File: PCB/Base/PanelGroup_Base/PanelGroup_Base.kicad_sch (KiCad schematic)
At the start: 62 parts, among them J1 J_DIAG, J11 J_BREAKOUT, J2 J_BL1, J3 J_I2C2, J4 J_I2C1, J5 J_CAN_TERM, J6 J_BL2, J7 J_SWD, J8 J_BUS_IN, J9 J_BUS_OUT, Q2 IRLML2502, Q3 IRLML2502, SW1 RESET, U1 STM32F103C8Tx, U2 SN65HVD230, U3 AMS1117-3.3, Y1 8MHz

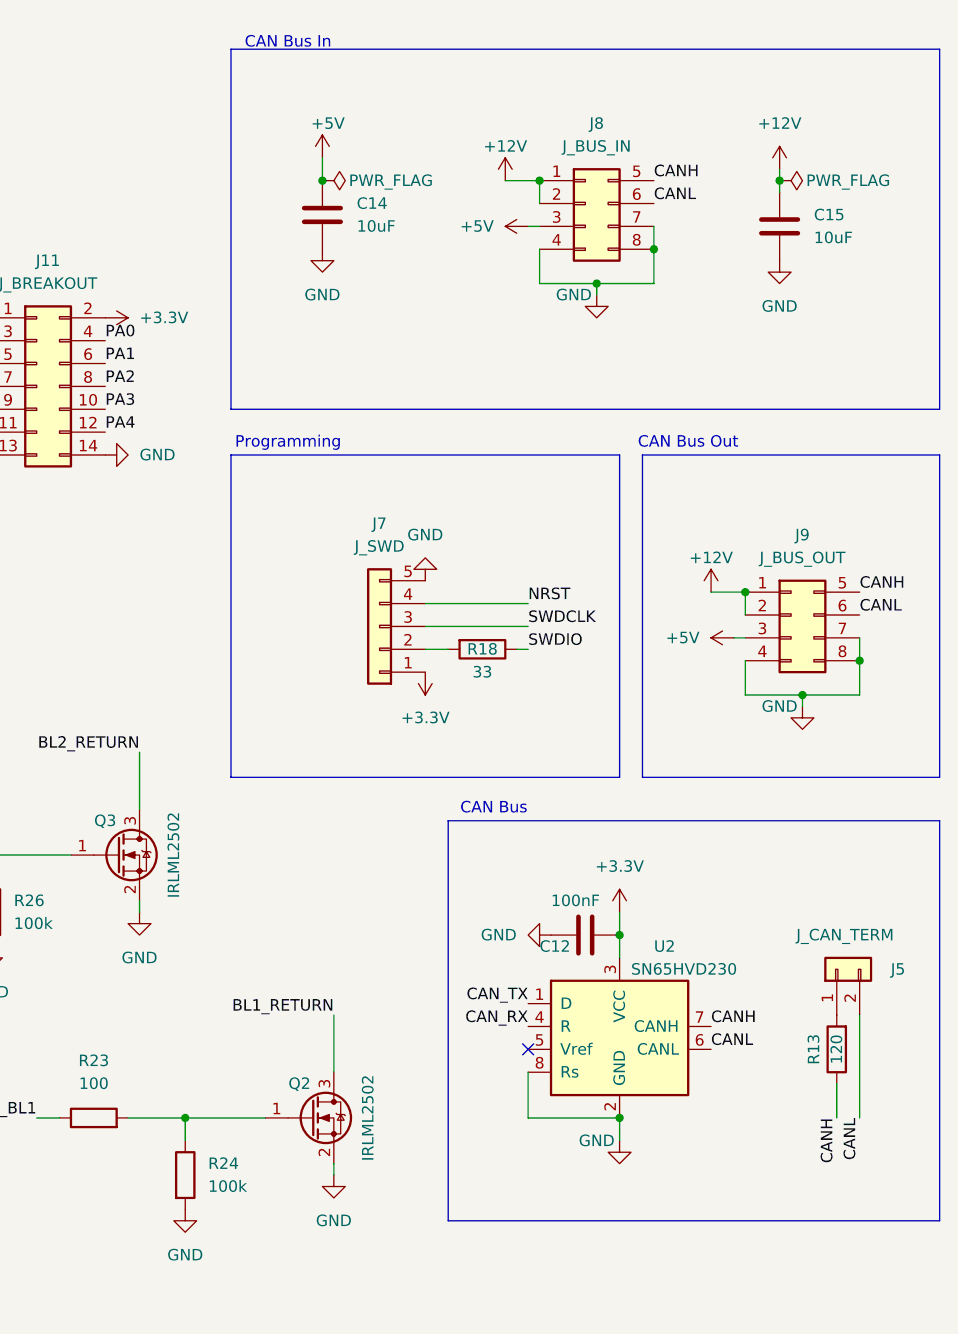
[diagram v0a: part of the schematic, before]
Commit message: feat(pcb): input-rail TVS + AO3400A backlight FET + 35V bus cap on base boards
Roll the #214 input-rail TVS fleet standard into both base boards, plus
two margin upgrades folded into the same rev:

- Input-rail TVS at J_BUS_IN on both boards: SMBJ12A (+12V, C42368008)
  and SMBJ6.0A (+5V, C5331096), cathode->rail / anode->GND, 2-3 GND
  vias at each anode pad for a low-inductance clamp path. CAN-bus TVS
  intentionally excluded (SN65HVD230 has built-in +/-16kV HBM).
- Backlight FET IRLML2502 -> AO3400A (C49195711, PanelGroup only):
  30V Vds vs 20V for headroom over the 19.9V clamp; Vgs operational at
  2.5V so still 3.3V-driven.
- +12V bulk cap C15 25V -> 35V X5R (C49010152): DC-bias derating +
  clamp headroom. C14 (+5V) stays 25V.

LCSC/MP/Voltage carried in-symbol. Combined BOM CSV + InvenTree updated.
DRC/ERC clean on both boards.

Refs #214
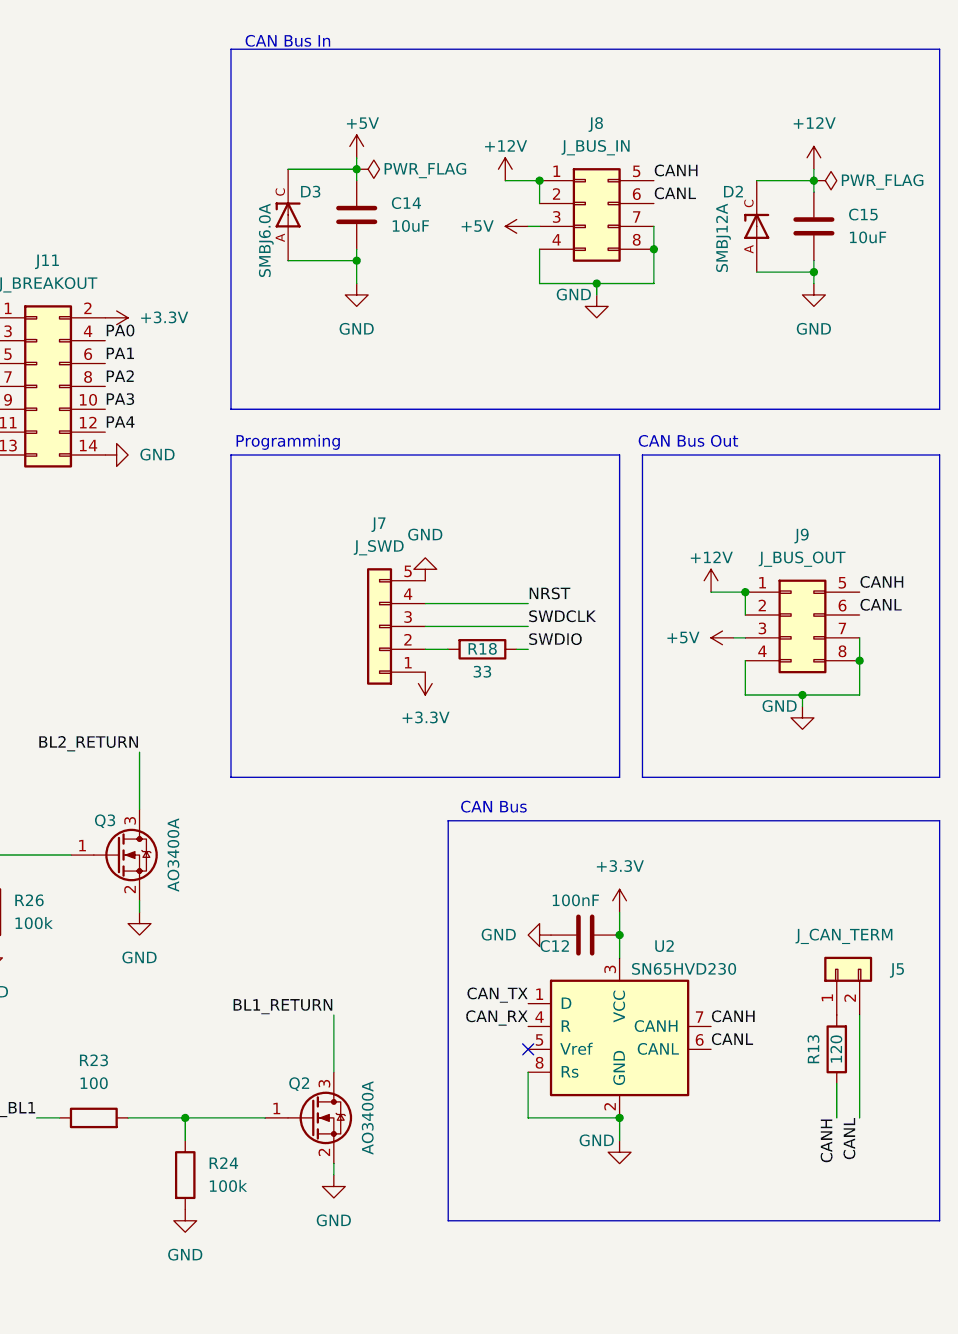
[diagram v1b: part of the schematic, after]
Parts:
- added D2: SMBJ12A, OpenSkyhawk:DIOM4336X265N, symbol OpenSkyhawk:SMBJ12A
- added D3: SMBJ6.0A, OpenSkyhawk:DIOM4336X265N, symbol OpenSkyhawk:SMBJ5.0A
- C15: LCSC (none) -> C49010152; Voltage (none) -> 35V
- Q2, Q3: value IRLML2502 -> AO3400A; LCSC (none) -> C49195711
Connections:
- net +12V: now also D2.C
- net +5V: now also D3.C
- net GND: now also D2.A, D3.A
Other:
- moved on the sheet: C14, C15

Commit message: feat(pcb): label base boards + PDU 1k downgrade to 1%
Extends the LCSC/tolerance/voltage labeling to the two base boards and
corrects a PDU over-spec.

- Gateway_Bridge, PanelGroup_Base: LCSC + tolerance + voltage on all
  parts (footprints already present). 10uF split 25V/35V by +12V rail.
  RP2040-Zero left blank (module, ordered separately, no LCSC); pin
  headers hand-soldered (no assembly LCSC).
- PDU: R8-R12/R15-R17 (1k series/anti-alias) downgraded C110774 0.1%
  -> C844939 1%. Precision belongs only on the divider ratio resistors
  (33k/13k/10k); the series 1k sit into high-Z ADC pins where 1% reads
  identically. Drops the precision C110774 from the board entirely.
- DESIGN-NOTES: record the 1k downgrade + the order-time shunt upgrade
  (C346481 100ppm -> C500740 25ppm).
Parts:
- C1, C12, C2, C3, C4, C5, C6, C9: LCSC (none) -> C1711; Rating (none) -> 50V; Tolerance (none) -> 10%
- C10: LCSC (none) -> C28323; Rating (none) -> 50V; Tolerance (none) -> 10%
- C11: LCSC (none) -> C3343; Rating (none) -> 25V; Tolerance (none) -> 20%
- C13: LCSC (none) -> C72502; Rating (none) -> 16V; Tolerance (none) -> 20%
- C14: LCSC (none) -> C669099; Rating (none) -> 25V; Tolerance (none) -> 20%
- C15: Rating (none) -> 35V; Tolerance (none) -> 20%
- C7, C8: LCSC (none) -> C1804; Rating (none) -> 50V; Tolerance (none) -> 5%
- D1, D5: LCSC (none) -> C19171393
- D4: LCSC (none) -> C19171391
- J1: LCSC (none) -> C51940188
- J2, J6: LCSC (none) -> C20608113
- J3, J4: LCSC (none) -> C23067548
- J8, J9: LCSC (none) -> C20608116
- Q2, Q3: Rating (none) -> 30V
- R1, R10, R9: LCSC (none) -> C844412; Rating (none) -> 1/8W; Tolerance (none) -> 1%
- R11, R12, R18, R21, R22: LCSC (none) -> C2090807; Rating (none) -> 1/8W; Tolerance (none) -> 1%
- R13: LCSC (none) -> C844816; Rating (none) -> 1/8W; Tolerance (none) -> 1%
- R16, R17, R19, R20, R23, R25: LCSC (none) -> C844936; Rating (none) -> 1/8W; Tolerance (none) -> 1%
- R2, R3, R4, R5: LCSC (none) -> C844941; Rating (none) -> 1/8W; Tolerance (none) -> 1%
- R24, R26: LCSC (none) -> C844935; Rating (none) -> 1/8W; Tolerance (none) -> 1%
- R6, R_BOOT1: LCSC (none) -> C844937; Rating (none) -> 1/8W; Tolerance (none) -> 1%
- SW1: LCSC (none) -> C2939600
- U1: LCSC (none) -> C8734
- U2: LCSC (none) -> C12084
- U3: LCSC (none) -> C347222
- Y1: LCSC (none) -> C20617997

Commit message: chore(pcb): normalize passive value-string case fleet-wide
Cosmetic cleanup — standardize resistor/cap value strings so identical
parts stop showing as separate BOM lines. Value = magnitude only;
tolerance + LCSC carry the precision distinction.

- 10K -> 10k, 4.7K -> 4.7k, 100K -> 100k (lowercase SI k)
- 100nf -> 100nF
- 69 symbols across all 6 boards (ASN-41, ARC-51A, APN-153, PDU,
  Gateway_Bridge, PanelGroup_Base). ERC 0/0 on all.

No functional/footprint/LCSC change. PDU generic 10k and precision
divider 10k now both read "10k", distinguished by tolerance (1% vs 0.1%).
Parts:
- C1: value 100nf -> 100nF
- R_BOOT1: value 10K -> 10k
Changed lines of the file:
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@@
 			)
 		)
-		(property "Value" "100nf"
+		(property "Value" "100nF"
 			(at 19.05 34.29 0)
 			(show_name no)
@@
 			)
 		)
-		(property "Value" "10K"
+		(property "Value" "10k"
 			(at 22.86 59.69 0)
 			(show_name no)

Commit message: refactor(pcb): consolidate ceramic 10uF to single 35V part
The 10uF ceramic 0805 caps were split across two SKUs — C669099 (25V)
and C49010152 (35V) — distinguished only by rail. Standardize all 8
ceramic positions to the 35V part (C49010152); 35V covers the 25V
positions and collapses the BOM to one ceramic 10uF value.

Electrolytic 10uF (C3343) unchanged. Aluminum-bulk replacement deferred
to a future round. 8 caps across all 6 boards, ERC 0/0.
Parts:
- C14: LCSC C669099 -> C49010152; Rating 25V -> 35V
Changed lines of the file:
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@@
 			)
 		)
-		(property "Rating" "25V"
+		(property "Rating" "35V"
 			(at 215.9 35.56 0)
 			(hide yes)
@@
 			)
 		)
-		(property "LCSC" "C669099"
+		(property "LCSC" "C49010152"
 			(at 215.9 35.56 0)
 			(hide yes)

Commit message: fix(pcb): correct SMBJ6.0A TVS metadata on PDU/base boards
D2 (PDU), D6 (Gateway_Bridge), D3 (PanelGroup_Base) carried stale
SnapEDA metadata from the original SMBJ5.0A (Taiwan Semiconductor)
symbol after the value was swapped to the 6.0A part. Value + LCSC
(C5331096) were already correct; this aligns the rest so BOM/inventory
exports agree with InvenTree:
- MF Taiwan Semiconductor -> MSKSEMI (actual mfr of C5331096)
- MP SMBJ5.0A -> SMBJ6.0A (PDU; already correct on base boards)
- Description 5V -> 6V
- Purchase-URL -> LCSC product page; clear stale SnapEDA links,
  Taiwan-Semi PARTREV/Package refs

ERC clean on all three.
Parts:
- D3: Check_prices https://www.snapeda.com/parts/SMBJ5.0A/taiwan/view-part/?re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 -> (none); MF Taiwan Semiconductor -> MSKSEMI; PARTREV F2102 -> NA; Package SMD-2 Taiwan Semiconductor -> SMD-2; Purchase-URL https://www.snapeda.com/api/url_track_click_mouser/?unipart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 -> https://www.lcsc.com/product-detail/TVS_Diodes_MSKSEMI_SMBJ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; SnapEDA_Link https://www.snapeda.com/parts/SMBJ5.0A/taiwan/view-part/?re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 -> (none)
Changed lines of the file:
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@@
 			)
 		)
-		(property "Description" "600W, 5V, Unidirectional, TVS"
+		(property "Description" "600W, 6V, Unidirectional, TVS"
 			(at 208.28 35.56 0)
 			(hide yes)
@@
 			)
 		)
-		(property "MF" "Taiwan Semiconductor"
+		(property "MF" "MSKSEMI"
 			(at 208.28 35.56 0)
 			(hide yes)
@@
 			)
 		)
-		(property "Package" "SMD-2 Taiwan Semiconductor"
+		(property "Package" "SMD-2"
 			(at 208.28 35.56 0)
 			(hide yes)
@@
 			)
 		)
-		(property "Check_prices" "https://www.snapeda.com/parts/SMBJ5.0A/taiwan/view-part/?ref=eda"
+		(property "Check_prices" ""
 			(at 208.28 35.56 0)
 			(hide yes)
@@
 			)
 		)
-		(property "PARTREV" "F2102"
+		(property "PARTREV" "NA"
 			(at 208.28 35.56 0)
 			(hide yes)
@@
 			)
 		)
-		(property "SnapEDA_Link" "https://www.snapeda.com/parts/SMBJ5.0A/taiwan/view-part/?ref=snap"
+		(property "SnapEDA_Link" ""
 			(at 208.28 35.56 0)
 			(hide yes)
@@
 			)
 		)
-		(property "Purchase-URL" "https://www.snapeda.com/api/url_track_click_mouser/?unipart_id=1860032&manufacturer=Taiwan Semiconductor&part_name=SMBJ5.0A&search_term=smbj5.0a"
+		(property "Purchase-URL" "https://www.lcsc.com/product-detail/TVS_Diodes_MSKSEMI_SMBJ6.0A_C5331096.html"
 			(at 208.28 35.56 0)
 			(hide yes)

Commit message: fix(pcb): re-value AMS1117 input ceramic 10uF->100nF (ASN/PDU/Gate/Pane)
The AMS1117 +5V input carried two bulk caps (10uF ceramic + 10uF elec)
and no HF bypass. Re-value the redundant 10uF ceramic to 100nF (reuse
C1711, 0805 unchanged) so each input = 10uF elec bulk + 100nF ceramic
HF = standard LDO input. No footprint/symbol change; ERC clean.
Frees another 10uF/35V ceramic and closes the missing-input-HF gap.
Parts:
- C14: value 10uF -> 100nF; LCSC C49010152 -> C1711; Rating 35V -> 50V; Tolerance 20% -> 10%
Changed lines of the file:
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@@
 			)
 		)
-		(property "Value" "10uF"
+		(property "Value" "100nF"
 			(at 219.71 36.8299 0)
 			(show_name no)
@@
 			)
 		)
-		(property "Rating" "35V"
+		(property "Rating" "50V"
 			(at 215.9 35.56 0)
 			(hide yes)
@@
 			)
 		)
-		(property "Tolerance" "20%"
+		(property "Tolerance" "10%"
 			(at 215.9 35.56 0)
 			(hide yes)
@@
 			)
 		)
-		(property "LCSC" "C49010152"
+		(property "LCSC" "C1711"
 			(at 215.9 35.56 0)
 			(hide yes)

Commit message: feat(pcb): add descriptive IPN field to all on-board symbols (#238 Phase 3) (#239)
Phase 3 of the IPN convention (#238): adds a stable, descriptive
**Internal Part Number** to every on-board symbol, co-equal with LCSC.
BOMs now anchor on a fixed identity; the LCSC can change with
availability without altering the part's identity.

## What changed
- **352 symbols** across all 6 boards (multi-sheet aware) get an `IPN`
field. **51 distinct IPNs.** ERC clean fleet-wide.
- **Off-board controls** (encoders/switches/pots/OLED/stepper — no
footprint, connector-coupled) get **no IPN**, per the standing off-board
exclusion. On-board modules (RP2040-ZERO) and the RESET tact switch
**do** get IPNs.
- `.gitignore`: FreeCAD backups (`*.FCBak`/`*.FCStd1`) + KiCad ERC/DRC
reports (`*-erc.rpt`/`*-drc.rpt`).

## Scheme (descriptive, locked in #238)
`RES-10K-1PCT-0805` · `CAP-CER-100NF-50V-0805` · `CAP-ELEC-22UF-16V-D4`
· `IC-STM32F103C8-LQFP` · `CONN-XH-8P` · `TVS-SMBJ12A-SMB` ·
`FUSE-HOLDER-BLADE-DIP4` · `SW-TACT-6MM` · `MOD-RP2040-ZERO`.

Resolved the 3 open encoding items: ferrite → `FB-600R-0805` (TDK
600Ω@100MHz), NTC → `NTC-10K-1206` (APV 10K), fuse holder (C19727305 is
a *holder*, not a fuse) → one `FUSE-HOLDER-BLADE-DIP4`.

## Not in this PR (later phases of #238)
- **Phase 2 — InvenTree:** set the IPN field + link SupplierParts incl
backorder alternates (one IPN → many LCSC). This is what actually
delivers the churn-proofing; needs reviewed InvenTree writes.
- **Phase 4 — order flow:** resolve IPN → in-stock LCSC at order time.

Refs #238.
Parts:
- C1, C12, C14, C2, C3, C4, C5, C6, C9: IPN (none) -> CAP-CER-100NF-50V-0805
- C10: IPN (none) -> CAP-CER-1UF-50V-0805
- C11: IPN (none) -> CAP-ELEC-10UF-25V-D4
- C13: IPN (none) -> CAP-ELEC-22UF-16V-D4
- C15: IPN (none) -> CAP-CER-10UF-35V-0805
- C7, C8: IPN (none) -> CAP-C0G-22PF-50V-0805
- D1, D5: IPN (none) -> LED-GREEN-0805
- D2: IPN (none) -> TVS-SMBJ12A-SMB
- D3: IPN (none) -> TVS-SMBJ6V0A-SMB
- D4: IPN (none) -> LED-RED-0805
- J1: IPN (none) -> CONN-XH-3P
- J11, J5: IPN (none) -> CONN-HDR-2P
- J2, J6: IPN (none) -> CONN-MF-2P
- J3, J4: IPN (none) -> CONN-XH-8P
- J7: IPN (none) -> CONN-HDR-5P
- J8, J9: IPN (none) -> CONN-MF-8P
- Q2, Q3: IPN (none) -> Q-AO3400A-SOT23
- R1, R10, R9: IPN (none) -> RES-3K3-1PCT-0805
- R11, R12, R18, R21, R22: IPN (none) -> RES-33R-1PCT-0805
- R13: IPN (none) -> RES-120R-1PCT-0805
- R16, R17, R19, R20, R23, R25: IPN (none) -> RES-100R-1PCT-0805
- R2, R3, R4, R5: IPN (none) -> RES-4K7-1PCT-0805
- R24, R26: IPN (none) -> RES-100K-1PCT-0805
- R6, R_BOOT1: IPN (none) -> RES-10K-1PCT-0805
- SW1: IPN (none) -> SW-TACT-6MM
- U1: IPN (none) -> IC-STM32F103C8-LQFP
- U2: IPN (none) -> IC-SN65HVD230-SOIC
- U3: IPN (none) -> IC-AMS1117-3V3-SOT223
- Y1: IPN (none) -> XTAL-8MHZ-SMD5032
